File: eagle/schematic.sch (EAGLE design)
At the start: 23 parts, among them IC1 PIC18F1320SO, U1 MIC5205, U2 SG-3040LCLC

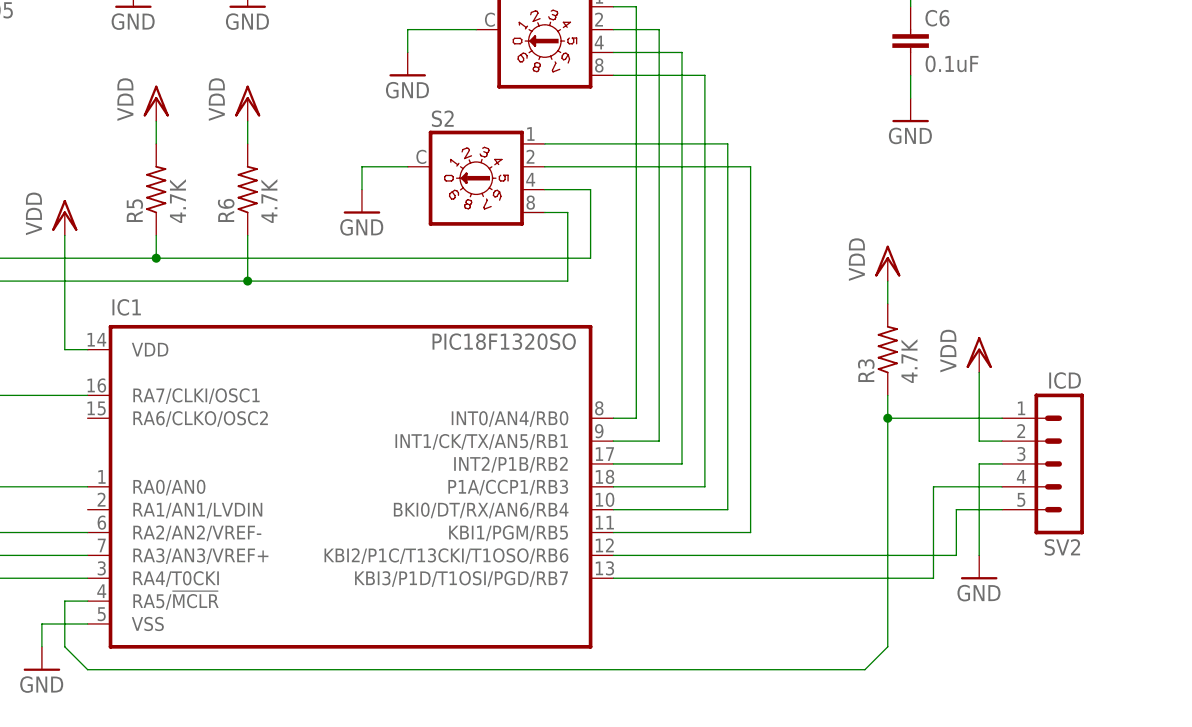
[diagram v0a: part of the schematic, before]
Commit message: Replaced ICD board header with a JST-EH connector
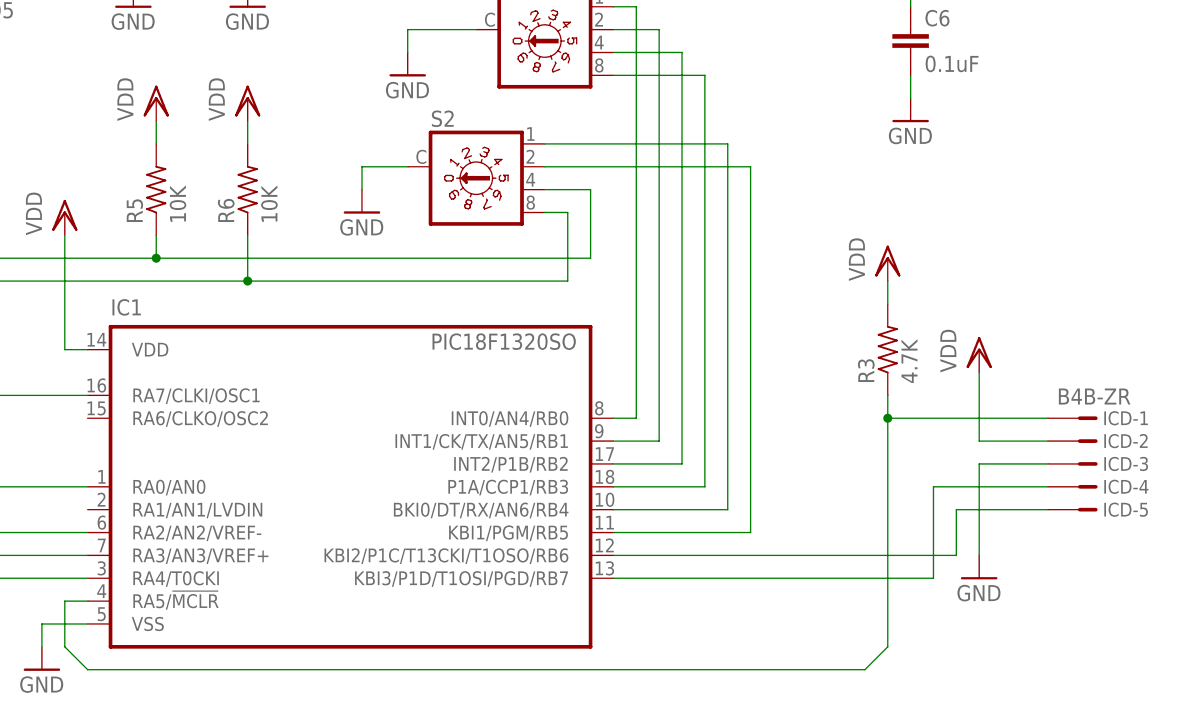
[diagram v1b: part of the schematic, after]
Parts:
- removed SV2: ICD, con-lstb:MA05-1
- added ICD: B4B-ZR, untitled:B4B-ZR
- R5, R6: value 4.7K -> 10K
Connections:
- net GND: now also ICD-3.1; no longer SV2.3
- net N$6: now also ICD-1.1; no longer SV2.1
- net N$7: now also ICD-4.1; no longer SV2.4
- net N$8: now also ICD-5.1; no longer SV2.5
- net VDD: now also ICD-2.1; no longer SV2.2
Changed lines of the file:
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@@
 <part name="VDD4" library="supply1" deviceset="VDD" device=""/>
 <part name="GND10" library="supply1" deviceset="GND" device=""/>
-<part name="SV2" library="con-lstb" deviceset="MA05-1" device="" value="ICD"/>
 <part name="R3" library="resistor" deviceset="R-US_" device="0204/2V" value="4.7K"/>
 <part name="VDD5" library="supply1" deviceset="VDD" device=""/>
@@
 <part name="GND14" library="supply1" deviceset="GND" device=""/>
 <part name="GND15" library="supply1" deviceset="GND" device=""/>
-<part name="R5" library="resistor" deviceset="R-US_" device="0204/2V" value="4.7K"/>
-<part name="R6" library="resistor" deviceset="R-US_" device="0204/2V" value="4.7K"/>
+<part name="R5" library="resistor" deviceset="R-US_" device="0204/2V" value="10K"/>
+<part name="R6" library="resistor" deviceset="R-US_" device="0204/2V" value="10K"/>
 <part name="VDD7" library="supply1" deviceset="VDD" device=""/>
 <part name="VDD8" library="supply1" deviceset="VDD" device=""/>
 <part name="GND7" library="supply1" deviceset="GND" device=""/>
+<part name="ICD" library="untitled" deviceset="?4B-ZR" device="B"/>
 </parts>
 <sheets>
@@
 <instance part="VDD4" gate="G$1" x="162.56" y="68.58"/>
 <instance part="GND10" gate="1" x="162.56" y="43.18"/>
-<instance part="SV2" gate="G$1" x="172.72" y="55.88" rot="R180"/>
 <instance part="R3" gate="G$1" x="152.4" y="68.58" rot="R90"/>
 <instance part="VDD5" gate="G$1" x="152.4" y="78.74"/>
@@
 <instance part="VDD8" gate="G$1" x="81.28" y="96.52"/>
 <instance part="GND7" gate="1" x="12.7" y="99.06"/>
+<instance part="ICD" gate="-5" x="175.26" y="50.8"/>
+<instance part="ICD" gate="-1" x="175.26" y="60.96"/>
+<instance part="ICD" gate="-2" x="175.26" y="58.42"/>
+<instance part="ICD" gate="-3" x="175.26" y="55.88"/>
+<instance part="ICD" gate="-4" x="175.26" y="53.34"/>
 </instances>
 <busses>
@@
 <segment>
 <pinref part="GND10" gate="1" pin="GND"/>
-<pinref part="SV2" gate="G$1" pin="3"/>
-<wire x1="165.1" y1="55.88" x2="162.56" y2="55.88" width="0.1524" layer="91"/>
 <wire x1="162.56" y1="55.88" x2="162.56" y2="45.72" width="0.1524" layer="91"/>
+<pinref part="ICD" gate="-3" pin="1"/>
+<wire x1="162.56" y1="55.88" x2="170.18" y2="55.88" width="0.1524" layer="91"/>
 </segment>
 <segment>
@@
 <wire x1="162.56" y1="58.42" x2="162.56" y2="66.04" width="0.1524" layer="91"/>
 <pinref part="VDD4" gate="G$1" pin="VDD"/>
-<pinref part="SV2" gate="G$1" pin="2"/>
-<wire x1="165.1" y1="58.42" x2="162.56" y2="58.42" width="0.1524" layer="91"/>
+<pinref part="ICD" gate="-2" pin="1"/>
+<wire x1="162.56" y1="58.42" x2="170.18" y2="58.42" width="0.1524" layer="91"/>
 </segment>
 <segment>
@@
 <wire x1="149.86" y1="33.02" x2="152.4" y2="35.56" width="0.1524" layer="91"/>
 <wire x1="152.4" y1="35.56" x2="152.4" y2="60.96" width="0.1524" layer="91"/>
-<pinref part="SV2" gate="G$1" pin="1"/>
-<wire x1="152.4" y1="60.96" x2="165.1" y2="60.96" width="0.1524" layer="91"/>
 <junction x="152.4" y="60.96"/>
 <pinref part="R3" gate="G$1" pin="1"/>
 <wire x1="152.4" y1="60.96" x2="152.4" y2="63.5" width="0.1524" layer="91"/>
+<pinref part="ICD" gate="-1" pin="1"/>
+<wire x1="152.4" y1="60.96" x2="170.18" y2="60.96" width="0.1524" layer="91"/>
 </segment>
 </net>
@@
 <pinref part="IC1" gate="G$1" pin="KBI3/P1D/T1OSI/PGD/RB7"/>
 <wire x1="121.92" y1="43.18" x2="157.48" y2="43.18" width="0.1524" layer="91"/>
-<pinref part="SV2" gate="G$1" pin="4"/>
 <wire x1="157.48" y1="43.18" x2="157.48" y2="53.34" width="0.1524" layer="91"/>
-<wire x1="157.48" y1="53.34" x2="165.1" y2="53.34" width="0.1524" layer="91"/>
+<pinref part="ICD" gate="-4" pin="1"/>
+<wire x1="157.48" y1="53.34" x2="170.18" y2="53.34" width="0.1524" layer="91"/>
 </segment>
 </net>
@@
 <segment>
 <pinref part="IC1" gate="G$1" pin="KBI2/P1C/T13CKI/T1OSO/RB6"/>
-<pinref part="SV2" gate="G$1" pin="5"/>
 <wire x1="121.92" y1="45.72" x2="160.02" y2="45.72" width="0.1524" layer="91"/>
 <wire x1="160.02" y1="45.72" x2="160.02" y2="50.8" width="0.1524" layer="91"/>
-<wire x1="160.02" y1="50.8" x2="165.1" y2="50.8" width="0.1524" layer="91"/>
-</segment>
-</net>
+<pinref part="ICD" gate="-5" pin="1"/>
+<wire x1="160.02" y1="50.8" x2="170.18" y2="50.8" width="0.1524" layer="91"/>
+</segment>
+</net>

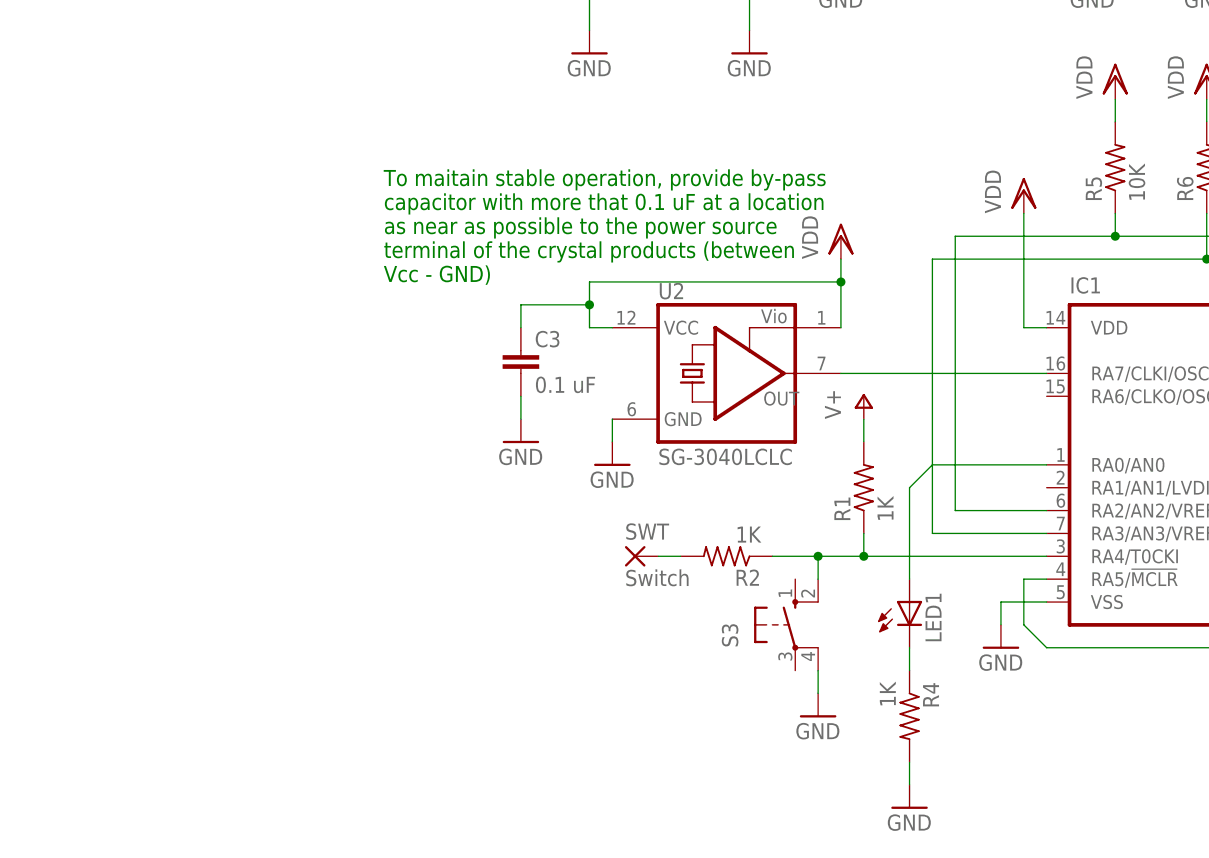
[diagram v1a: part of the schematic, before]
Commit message: Added larger JC variant of oscillator to the underside of the PCB
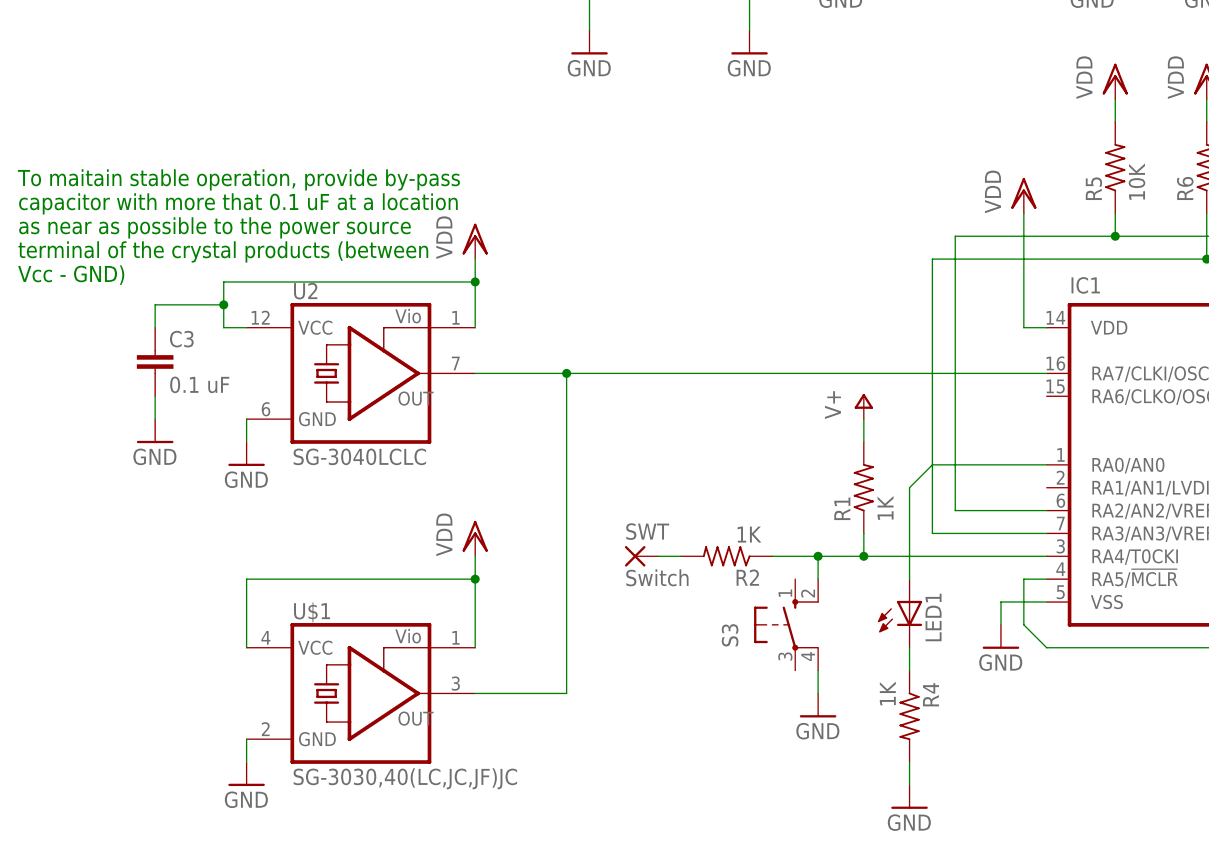
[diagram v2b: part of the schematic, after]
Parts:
- added U$1: SG-3030,40(LC,JC,JF)JC, untitled:SG-3030,40(LC,JC,JF)JC
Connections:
- net CLK: now also U$1.OUT
- net GND: now also U$1.GND
- net VDD: now also U$1.VCC, U$1.VIO
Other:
- moved on the sheet: C3, U2

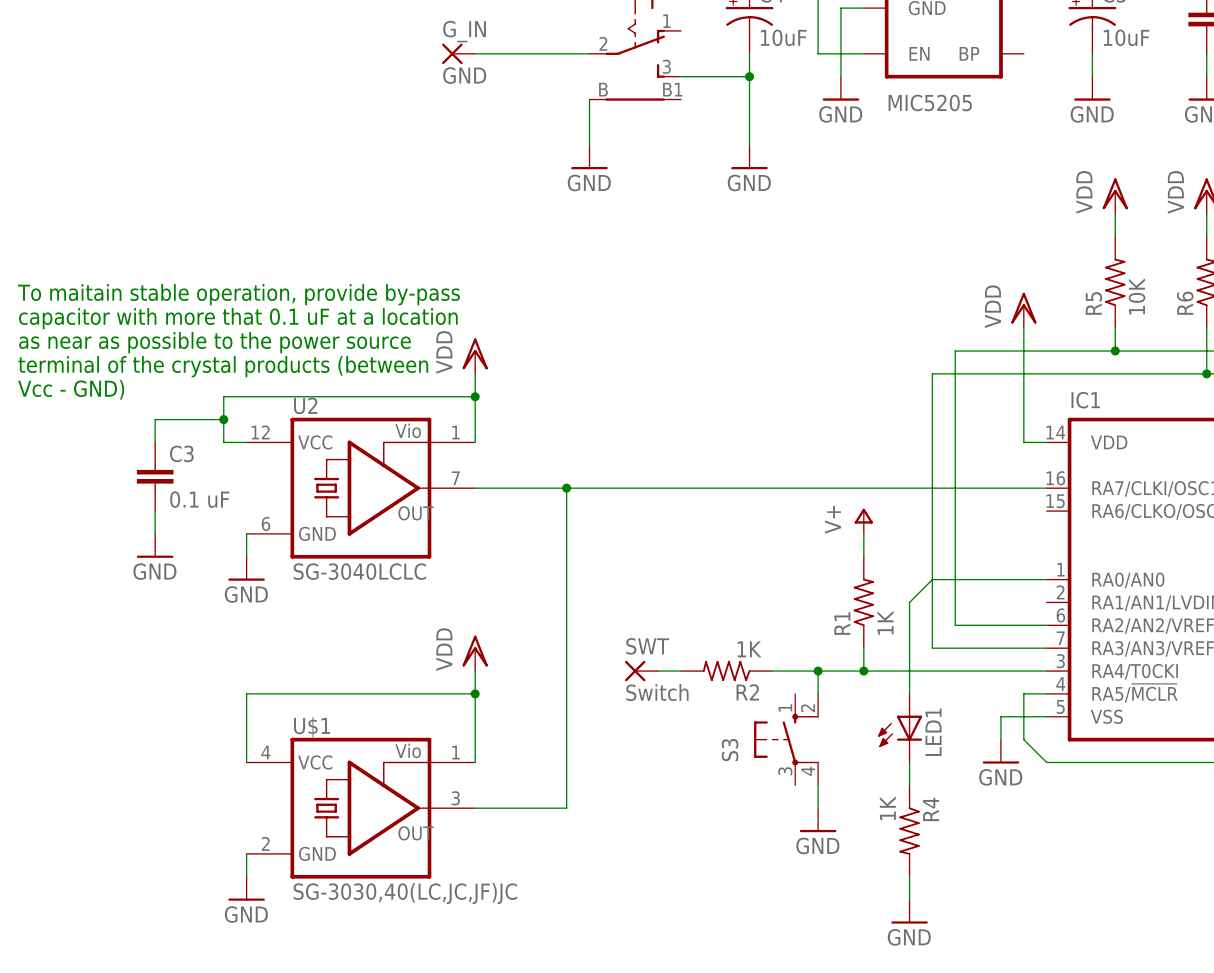
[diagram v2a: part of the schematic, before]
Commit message: Redo layout of extra oscillator
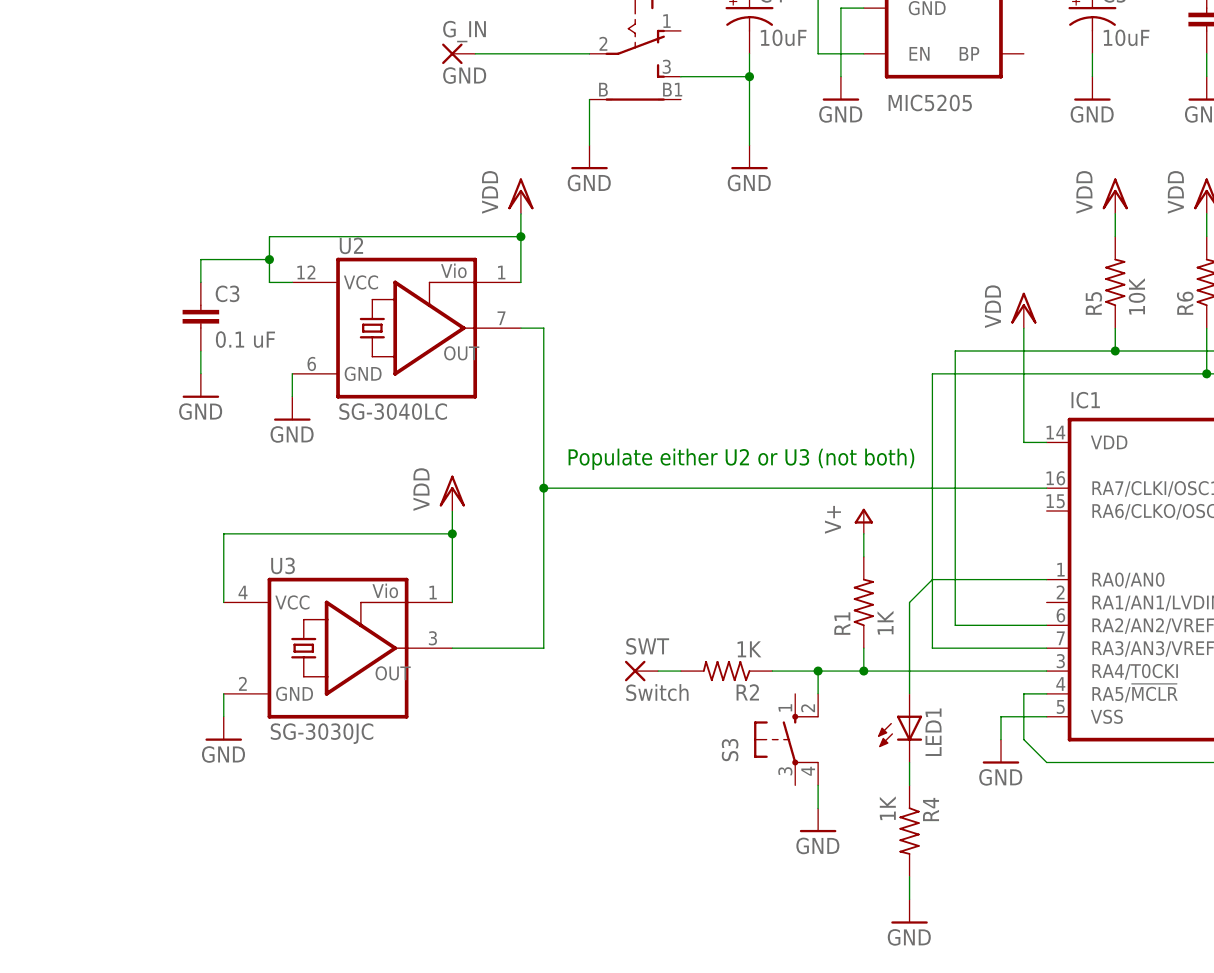
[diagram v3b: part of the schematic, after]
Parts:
- removed U$1: SG-3030,40(LC,JC,JF)JC, untitled:SG-3030,40(LC,JC,JF)JC
- added U3: SG-3030JC, untitled:SG-3030,40(LC,JC,JF)JC
- U2: value SG-3040LCLC -> SG-3040LC
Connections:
- net CLK: now also U3.OUT; no longer U$1.OUT
- net GND: now also U3.GND; no longer U$1.GND
- net VDD: now also U3.VCC, U3.VIO; no longer U$1.VCC, U$1.VIO
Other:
- note added: "Populate either U2 or U3 (not both)"
- note removed: "To maitain stable operation, provide by-pass capacitor with more that 0.1 uF at a location as near as possible to the power source terminal of the crystal products (between Vcc - GND)"
- moved on the sheet: C3, U2

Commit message: Files missing from the previous commit
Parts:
- C3: value 0.1 uF -> 0.22uF
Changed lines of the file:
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@@
 <part name="U2" library="untitled" deviceset="SG-3040LC" device="LC" value="SG-3040LC"/>
 <part name="GND3" library="supply1" deviceset="GND" device=""/>
-<part name="C3" library="capacitor-wima" deviceset="C" device="2,5-3" value="0.1 uF"/>
+<part name="C3" library="capacitor-wima" deviceset="C" device="2,5-3" value="0.22uF"/>
 <part name="C4" library="SparkFun" deviceset="CAP_POL" device="1206" value="10uF"/>
 <part name="C5" library="SparkFun" deviceset="CAP_POL" device="1206" value="10uF"/>
